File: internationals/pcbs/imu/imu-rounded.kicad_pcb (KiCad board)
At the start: 2 copper layers, 152.6 x 142 mm, 69 parts, among them J1 5V-JST-XH-B2B, J2 5V-JST-XH-B2B, J3 5V-JST-XH-B2B, J4 IMU-JST-XH-B4B, J5 BT-UART-JST-XH-B4B, J6 Top-UART-JST-XH-B2B, J7 Breakout-Header-01x04, J8 Breakout-Header-01x04, J9 Breakout-Header-01x02, SW1 SW_Push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

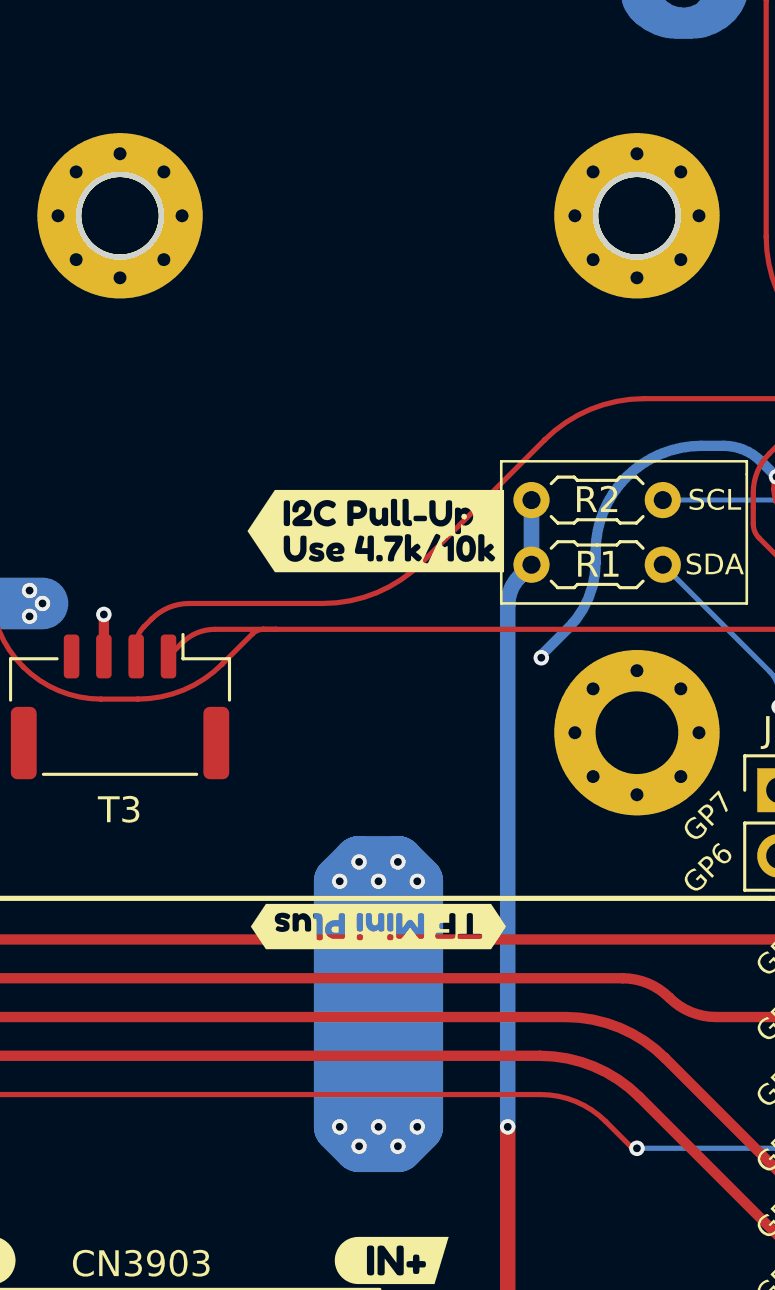
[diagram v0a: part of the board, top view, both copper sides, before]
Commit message: pcbs: feat: add OSHW and Rust Ferris logos
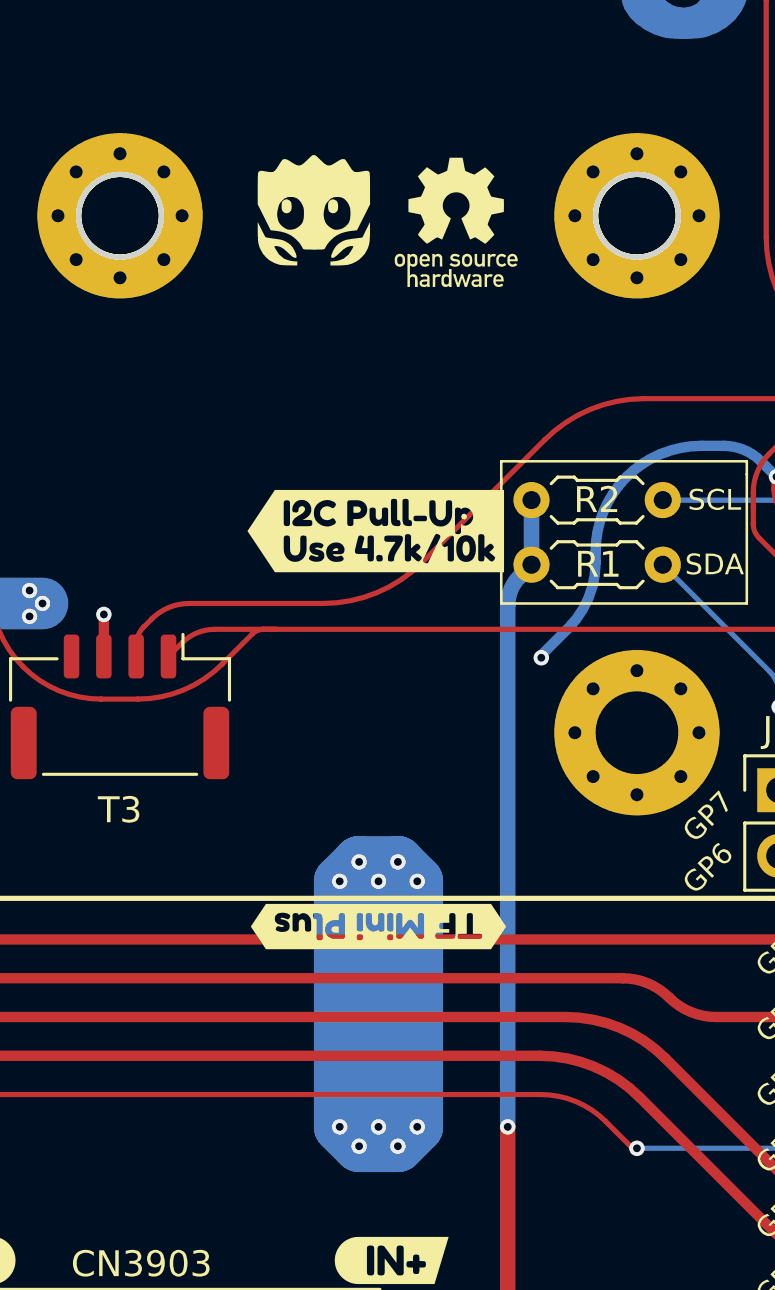
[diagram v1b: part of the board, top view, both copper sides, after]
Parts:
- added G***: LOGO, LOGO, F.Cu at (97.5, 99.8)
- added G***: LOGO, LOGO, F.Cu at (103.0, 100.2)
